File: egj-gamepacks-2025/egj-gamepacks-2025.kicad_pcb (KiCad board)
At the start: 2 copper layers, 55.7 x 32 mm, 44 parts, among them J1 USB_B_Micro, J3 SM03B-SRSS-TB, J5 GameBoy_GamePak_AGB-002, SW1 SW_Push, SW2 SW_Push, U1 W25Q128JVS, U2 DNF, U3 NCP1117-3.3_SOT223, U4 RP2350_80QFN, Y1 ABM8-272-T3

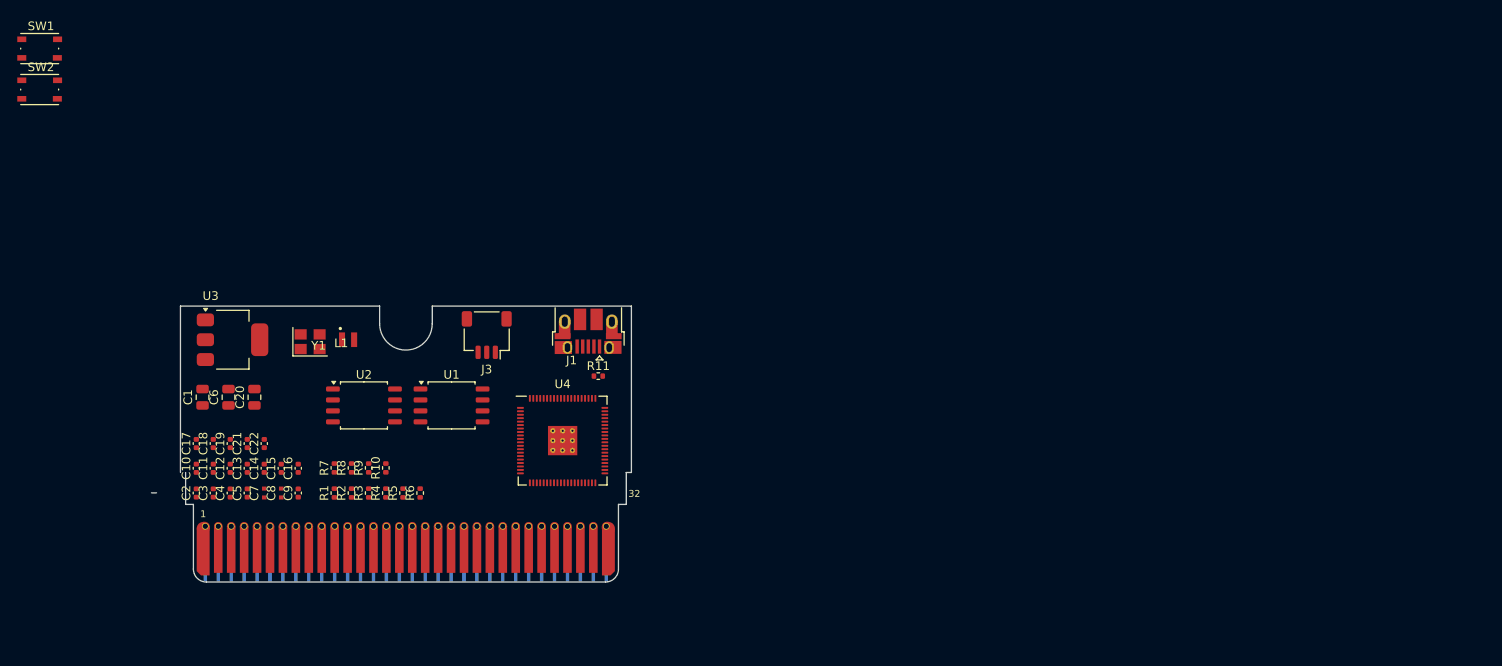
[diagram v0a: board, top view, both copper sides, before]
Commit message: add new schemas
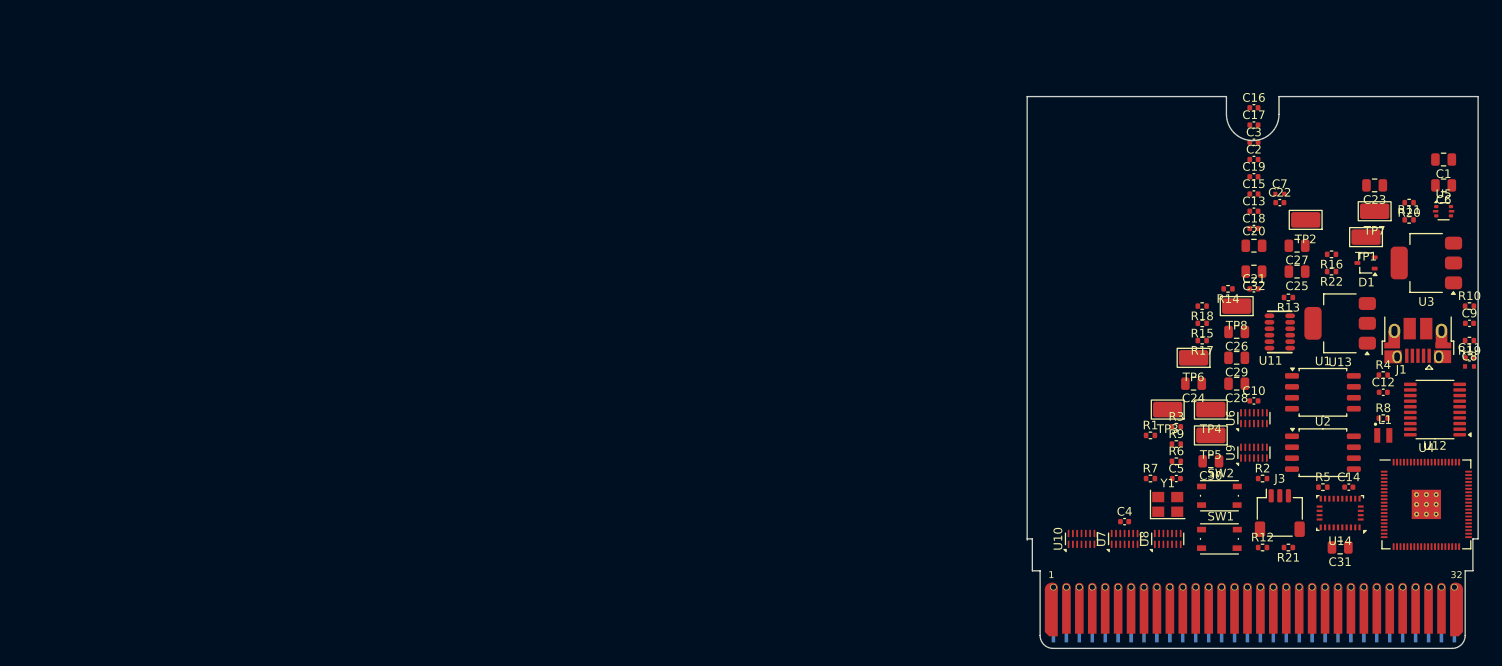
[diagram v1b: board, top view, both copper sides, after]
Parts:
- added C23: 100u, Capacitor_SMD:C_0805_2012Metric, F.Cu at (262.0, 71.0)
- added C24: 10u, Capacitor_SMD:C_0805_2012Metric, F.Cu at (241.0, 94.0)
- added C25: 100n, Capacitor_SMD:C_0805_2012Metric, F.Cu at (253.0, 81.0)
- added C26: 1u, Capacitor_SMD:C_0805_2012Metric, F.Cu at (246.0, 88.0)
- added C27: 1u, Capacitor_SMD:C_0805_2012Metric, F.Cu at (253.0, 78.0)
- added C28: 100n, Capacitor_SMD:C_0805_2012Metric, F.Cu at (246.0, 94.0)
- added C29: 4.7u, Capacitor_SMD:C_0805_2012Metric, F.Cu at (246.0, 91.0)
- added C30: 1u, Capacitor_SMD:C_0805_2012Metric, F.Cu at (243.0, 103.0)
- added C31: 120n, Capacitor_SMD:C_0805_2012Metric, F.Cu at (258.0, 113.0)
- added C32: 100n, Capacitor_SMD:C_0805_2012Metric, F.Cu at (248.0, 81.0)
- added D1: BAT54CW, Package_TO_SOT_SMD:SOT-323_SC-70, F.Cu at (261.0, 80.0)
- added R12: 10k, Resistor_SMD:R_0402_1005Metric, F.Cu at (249.0, 113.0)
- added R13: 4.7K, Resistor_SMD:R_0402_1005Metric, F.Cu at (252.0, 84.0)
- added R14: 4.7K, Resistor_SMD:R_0402_1005Metric, F.Cu at (245.0, 83.0)
- added R15: 33, Resistor_SMD:R_0402_1005Metric, F.Cu at (242.0, 87.0)
- added R16: 33, Resistor_SMD:R_0402_1005Metric, F.Cu at (257.0, 79.0)
- added R17: 4.7K, Resistor_SMD:R_0402_1005Metric, F.Cu at (242.0, 89.0)
- added R18: 4.7K, Resistor_SMD:R_0402_1005Metric, F.Cu at (242.0, 85.0)
- added R19: 4.7K, Resistor_SMD:R_0402_1005Metric, F.Cu at (273.0, 89.0)
- added R20: 10K, Resistor_SMD:R_0402_1005Metric, F.Cu at (266.0, 73.0)
- added R21: 4.7K, Resistor_SMD:R_0402_1005Metric, F.Cu at (252.0, 113.0)
- added R22: 10K, Resistor_SMD:R_0402_1005Metric, F.Cu at (257.0, 81.0)
- added TP1: TestPoint, TestPoint:TestPoint_Keystone_5015_Micro_Mini, F.Cu at (261.0, 77.0)
- added TP2: TestPoint, TestPoint:TestPoint_Keystone_5015_Micro_Mini, F.Cu at (254.0, 75.0)
- added TP3: TestPoint, TestPoint:TestPoint_Keystone_5015_Micro_Mini, F.Cu at (238.0, 97.0)
- added TP4: TestPoint, TestPoint:TestPoint_Keystone_5015_Micro_Mini, F.Cu at (243.0, 97.0)
- added TP5: TestPoint, TestPoint:TestPoint_Keystone_5015_Micro_Mini, F.Cu at (243.0, 100.0)
- added TP6: TestPoint, TestPoint:TestPoint_Keystone_5015_Micro_Mini, F.Cu at (241.0, 91.0)
- added TP7: TestPoint, TestPoint:TestPoint_Keystone_5015_Micro_Mini, F.Cu at (262.0, 74.0)
- added TP8: TestPoint, TestPoint:TestPoint_Keystone_5015_Micro_Mini, F.Cu at (246.0, 85.0)
- added U10: SP3012-06UTG, Package_DFN_QFN:DFN-14_1.35x3.5mm_P0.5mm, F.Cu at (228.0, 112.0)
- added U11: VL6180XV0NR_1, VL6180XV0NR_1:LGA12R75P2X6_280X480X110, F.Cu at (251.0, 88.0)
- added U12: TXS0108EPW, Package_SO:TSSOP-20_4.4x6.5mm_P0.65mm, F.Cu at (269.0, 97.0)
- added U13: LD1117S18TR_SOT223, Package_TO_SOT_SMD:SOT-223-3_TabPin2, F.Cu at (258.0, 87.0)
- added U14: BNO055, Package_LGA:LGA-28_5.2x3.8mm_P0.5mm, F.Cu at (258.0, 109.0)
- added U5: USBLC6-2P6, Package_TO_SOT_SMD:SOT-666, F.Cu at (270.0, 74.0)
- added U6: SP3012-06UTG, Package_DFN_QFN:DFN-14_1.35x3.5mm_P0.5mm, F.Cu at (248.0, 98.0)
- added U7: SP3012-06UTG, Package_DFN_QFN:DFN-14_1.35x3.5mm_P0.5mm, F.Cu at (233.0, 112.0)
- added U8: SP3012-06UTG, Package_DFN_QFN:DFN-14_1.35x3.5mm_P0.5mm, F.Cu at (238.0, 112.0)
- added U9: SP3012-06UTG, Package_DFN_QFN:DFN-14_1.35x3.5mm_P0.5mm, F.Cu at (248.0, 102.0)
- U1, U2: footprint Package_SO:SOIC-8_5.23x5.23mm_P1.27mm -> Package_SO:SOIC-8_5.3x5.3mm_P1.27mm
- moved SW1 148.2 mm to (244.0, 112.0)
- moved C1 146.6 mm to (270.0, 68.0), turned to 180 degrees
- moved C11 146.3 mm to (273.0, 91.0), turned to 0 degrees
- moved SW2 144.7 mm to (244.0, 107.0)
- moved C6 143.1 mm to (270.0, 71.0), turned to 180 degrees
- moved U3 138.7 mm to (268.0, 80.0), turned to 180 degrees
- moved C8 138.6 mm to (273.0, 92.0), turned to 0 degrees
- moved C9 137.3 mm to (273.0, 87.0), turned to 0 degrees
- moved C12 134.0 mm to (263.0, 95.0), turned to 0 degrees
- moved C2 128.6 mm to (248.0, 68.0), turned to 0 degrees
- moved C17 128.1 mm to (248.0, 64.0), turned to 0 degrees
- moved C3 127.4 mm to (248.0, 66.0), turned to 0 degrees
- moved R10 127.1 mm to (273.0, 85.0), turned to 0 degrees
- moved C14 125.8 mm to (259.0, 106.0), turned to 0 degrees
- moved C18 123.2 mm to (248.0, 76.0), turned to 0 degrees
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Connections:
- net /FLASH2_SS renamed /RP2350/FLASH2_SS
- net /FLASH_SS renamed /RP2350/FLASH_SS
- net /GPIO28 renamed /GBA_Connector/GBA_SIG.N_CS2
- net /GPIO29 renamed /GBA_Connector/GBA_SIG.IRQ
- net /QSPI_SCLK renamed /RP2350/QSPI_SCLK
- net /QSPI_SD0 renamed /RP2350/QSPI_SD0
- net /QSPI_SD1 renamed /RP2350/QSPI_SD1
- net /QSPI_SD2 renamed /RP2350/QSPI_SD2
- net /QSPI_SD3 renamed /RP2350/QSPI_SD3
- net /QSPI_SS renamed /RP2350/QSPI_SS
- net /RUN renamed /RP2350/RUN
- net /SWCLK renamed /RP2350/SWCLK
- net /SWD renamed /RP2350/SWD
- net /VREG_AVDD renamed Net-(U4-VREG_AVDD)
- net /VREG_LX renamed /RP2350/VREG_LX
- net /XIN renamed /RP2350/XIN
- net /XOUT renamed /RP2350/XOUT
- net /~{USB_BOOT} renamed /RP2350/~{USB_BOOT}
- C6 pad 1: +3V3 -> +3V3_USB
- J1 pad 2: /USB_D- -> /Power/USB.USB_D_C-
- J1 pad 3: /USB_D+ -> /Power/USB.USB_D_C+
- J5 pad 1: +3.3V -> +3V3_GBA
- J5 pad 10: /GPIO8 -> /GBA_Connector/GBA_ADD4
- J5 pad 11: /GPIO9 -> /GBA_Connector/GBA_ADD5
- J5 pad 12: /GPIO10 -> /GBA_Connector/GBA_ADD6
- J5 pad 13: /GPIO11 -> /GBA_Connector/GBA_ADD7
- J5 pad 14: /GPIO12 -> /GBA_Connector/GBA_ADD8
- J5 pad 15: /GPIO13 -> /GBA_Connector/GBA_ADD9
- J5 pad 16: /GPIO14 -> /GBA_Connector/GBA_ADD10
- J5 pad 17: /GPIO15 -> /GBA_Connector/GBA_ADD11
- J5 pad 18: /GPIO16 -> /GBA_Connector/GBA_ADD12
- J5 pad 19: /GPIO17 -> /GBA_Connector/GBA_ADD13
- J5 pad 2: /GPIO0 -> /GBA_Connector/GBA_SIG.PHI
- J5 pad 20: /GPIO18 -> /GBA_Connector/GBA_ADD14
- J5 pad 21: /GPIO19 -> /GBA_Connector/GBA_ADD15
- J5 pad 22: /GPIO20 -> /GBA_Connector/GBA_DATA0
- J5 pad 23: /GPIO21 -> /GBA_Connector/GBA_DATA1
- J5 pad 24: /GPIO22 -> /GBA_Connector/GBA_DATA2
- J5 pad 25: /GPIO23 -> /GBA_Connector/GBA_DATA3
- J5 pad 26: /GPIO24 -> /GBA_Connector/GBA_DATA4
- J5 pad 27: /GPIO25 -> /GBA_Connector/GBA_DATA5
- J5 pad 28: /GPIO26 -> /GBA_Connector/GBA_DATA6
- J5 pad 29: /GPIO27 -> /GBA_Connector/GBA_DATA7
- J5 pad 3: /GPIO1 -> /GBA_Connector/GBA_SIG.N_WR
- J5 pad 4: /GPIO2 -> /GBA_Connector/GBA_SIG.N_RD
- J5 pad 5: /GPIO3 -> /GBA_Connector/GBA_SIG.N_CS
- J5 pad 6: /GPIO4 -> /GBA_Connector/GBA_ADD0
- J5 pad 7: /GPIO5 -> /GBA_Connector/GBA_ADD1
- J5 pad 8: /GPIO6 -> /GBA_Connector/GBA_ADD2
- J5 pad 9: /GPIO7 -> /GBA_Connector/GBA_ADD3
- R1 pad 1: /GPIO0 -> /RP2350/GPIO0
- R10 pad 1: /USB_D+ -> /RP2350/USB_D+
- R11 pad 1: /USB_D- -> /RP2350/USB_D-
- R3 pad 1: /GPIO0 -> /RP2350/GPIO0
- U3 pad 2: +3V3 -> +3V3_USB
- U4 pad 1: /GPIO4 -> /GBA_Connector/GBA_DATA4
- U4 pad 11: /GPIO12 -> /GBA_Connector/GBA_ADD4
- U4 pad 12: /GPIO13 -> /GBA_Connector/GBA_ADD5
- U4 pad 13: /GPIO14 -> /GBA_Connector/GBA_ADD6
- U4 pad 14: /GPIO15 -> /GBA_Connector/GBA_ADD7
- U4 pad 16: /GPIO16 -> /GBA_Connector/GBA_ADD8
- U4 pad 17: /GPIO17 -> /GBA_Connector/GBA_ADD9
- U4 pad 18: /GPIO18 -> /GBA_Connector/GBA_ADD10
- U4 pad 19: /GPIO19 -> /GBA_Connector/GBA_ADD11
- U4 pad 2: /GPIO5 -> /GBA_Connector/GBA_DATA5
- U4 pad 20: /GPIO20 -> /GBA_Connector/GBA_ADD12
- U4 pad 21: /GPIO21 -> /GBA_Connector/GBA_ADD13
- U4 pad 22: /GPIO22 -> /GBA_Connector/GBA_ADD14
- U4 pad 23: /GPIO23 -> /GBA_Connector/GBA_ADD15
- U4 pad 25: /GPIO24 -> /GBA_Connector/GBA_SIG.PHI
- U4 pad 26: /GPIO25 -> /GBA_Connector/GBA_SIG.N_WR
- U4 pad 27: /GPIO26 -> /GBA_Connector/GBA_SIG.N_RD
- U4 pad 28: /GPIO27 -> /GBA_Connector/GBA_SIG.N_CS
- U4 pad 3: /GPIO6 -> /GBA_Connector/GBA_DATA6
- U4 pad 38: /GPIO30 -> /RP2350/VL6180XV0NR_I2C.SDA
- U4 pad 39: /GPIO31 -> /RP2350/VL6180XV0NR_I2C.SCL
- U4 pad 4: /GPIO7 -> /GBA_Connector/GBA_DATA7
- U4 pad 40: /GPIO32 -> /RP2350/VL6180XV0NR_I2C.GPIO0
- U4 pad 42: /GPIO33 -> /RP2350/VL6180XV0NR_I2C.GPIO1
- U4 pad 43: /GPIO34 -> unconnected-(U4-GPIO34-Pad43)
- U4 pad 44: /GPIO35 -> /RP2350/BNO055_UART.TX
- U4 pad 45: /GPIO36 -> /RP2350/BNO055_UART.RX
- U4 pad 46: /GPIO37 -> /RP2350/BNO055_UART.INT
- U4 pad 47: /GPIO38 -> /RP2350/BNO055_UART.RESET
- U4 pad 48: /GPIO39 -> /RP2350/BNO055_UART.BL_IND
- U4 pad 49: /GPIO40_ADC0 -> unconnected-(U4-GPIO40_ADC0-Pad49)
- U4 pad 52: /GPIO41_ADC1 -> unconnected-(U4-GPIO41_ADC1-Pad52)
- U4 pad 53: /GPIO42_ADC2 -> unconnected-(U4-GPIO42_ADC2-Pad53)
- U4 pad 54: /GPIO43_ADC3 -> unconnected-(U4-GPIO43_ADC3-Pad54)
- U4 pad 55: /GPIO44_ADC4 -> unconnected-(U4-GPIO44_ADC4-Pad55)
- U4 pad 56: /GPIO45_ADC5 -> unconnected-(U4-GPIO45_ADC5-Pad56)
- U4 pad 57: /GPIO46_ADC6 -> +3V3_GBA
- U4 pad 58: /GPIO47_ADC7 -> +3V3_USB
- U4 pad 6: /GPIO8 -> /GBA_Connector/GBA_ADD0
- U4 pad 7: /GPIO9 -> /GBA_Connector/GBA_ADD1
- U4 pad 77: /GPIO0 -> /GBA_Connector/GBA_DATA0
- U4 pad 78: /GPIO1 -> /GBA_Connector/GBA_DATA1
- U4 pad 79: /GPIO2 -> /GBA_Connector/GBA_DATA2
- U4 pad 8: /GPIO10 -> /GBA_Connector/GBA_ADD2
- U4 pad 80: /GPIO3 -> /GBA_Connector/GBA_DATA3
- U4 pad 9: /GPIO11 -> /GBA_Connector/GBA_ADD3
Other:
- board size 55.7 x 32 mm -> 52.3 x 64 mm

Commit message: Update
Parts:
- removed J3: SM03B-SRSS-TB, Connector_JST:JST_SH_SM03B-SRSS-TB_1x03-1MP_P1.00mm_Horizontal
- removed TP1, TP2, TP7, TP8: TestPoint, TestPoint:TestPoint_Keystone_5015_Micro_Mini
- added J2: Conn_01x03_Pin, Connector_PinHeader_2.54mm:PinHeader_1x03_P2.54mm_Horizontal, F.Cu at (119.0, 66.0)
- added U15: SP3012-06UTG, Package_DFN_QFN:DFN-14_1.35x3.5mm_P0.5mm, F.Cu at (165.0, 113.0)
- moved C9 140.2 mm to (133.2, 96.6), turned to 180 degrees
- moved C11 139.9 mm to (133.2, 94.6), turned to 180 degrees
- moved C8 139.9 mm to (133.1, 93.6), turned to 180 degrees
- moved R4 139.5 mm to (123.5, 94.0), turned to 180 degrees
- moved R19 133.6 mm to (139.6, 81.9), turned to 90 degrees
- moved R5 132.5 mm to (123.5, 102.5), turned to 180 degrees
- moved U1 131.5 mm to (124.5, 97.5)
- moved U2 131.5 mm to (124.6, 105.9)
- moved C12 129.8 mm to (133.2, 95.6), turned to 180 degrees
- moved R2 129.0 mm to (120.5, 94.0)
- moved SW1 128.6 mm to (125.5, 62.0)
- moved C3 127.8 mm to (125.5, 102.5)
- moved L1 127.4 mm to (135.7, 96.1)
- moved R10 126.7 mm to (147.4, 68.0), turned to -90 degrees
- moved U12 125.5 mm to (144.1, 84.4), turned to -90 degrees
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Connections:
- net +1V1 renamed /RP2350/+1V1
- D1 pad 1: +3V3_GBA -> +3V3_USB
- D1 pad 2: +3V3_USB -> +3V3_GBA
- R10 pad 1: /RP2350/USB_D+ -> /Power/USB.USB_D_C+
- R11 pad 1: /RP2350/USB_D- -> /Power/USB.USB_D_C-
- U10 pad 1: unconnected-(U10-Pad1) -> /GBA_Connector/GBA_ADD13
- U10 pad 11: /GBA_Connector/GBA_SIG.N_CS -> /GBA_Connector/GBA_DATA0
- U10 pad 12: /GBA_Connector/GBA_SIG.N_RD -> /GBA_Connector/GBA_ADD15
- U10 pad 13: /GBA_Connector/GBA_SIG.N_WR -> /GBA_Connector/GBA_ADD14
- U10 pad 14: /GBA_Connector/GBA_SIG.PHI -> /GBA_Connector/GBA_ADD13
- U10 pad 2: unconnected-(U10-Pad2) -> /GBA_Connector/GBA_ADD14
- U10 pad 3: unconnected-(U10-Pad3) -> /GBA_Connector/GBA_ADD15
- U10 pad 4: unconnected-(U10-Pad4) -> /GBA_Connector/GBA_DATA0
- U10 pad 5: unconnected-(U10-Pad5) -> GND
- U10 pad 6: unconnected-(U10-Pad6) -> /GBA_Connector/GBA_DATA1
- U10 pad 7: unconnected-(U10-Pad7) -> /GBA_Connector/GBA_DATA2
- U10 pad 8: /GBA_Connector/GBA_SIG.IRQ -> /GBA_Connector/GBA_DATA2
- U10 pad 9: /GBA_Connector/GBA_SIG.N_CS2 -> /GBA_Connector/GBA_DATA1
- U4 pad 1: /GBA_Connector/GBA_DATA4 -> /GBA_Connector/GBA_ADD0
- U4 pad 11: /GBA_Connector/GBA_ADD4 -> /GBA_Connector/GBA_ADD8
- U4 pad 12: /GBA_Connector/GBA_ADD5 -> /GBA_Connector/GBA_ADD9
- U4 pad 13: /GBA_Connector/GBA_ADD6 -> /GBA_Connector/GBA_ADD10
- U4 pad 14: /GBA_Connector/GBA_ADD7 -> /GBA_Connector/GBA_ADD11
- U4 pad 16: /GBA_Connector/GBA_ADD8 -> /GBA_Connector/GBA_ADD12
- U4 pad 17: /GBA_Connector/GBA_ADD9 -> /GBA_Connector/GBA_ADD13
- U4 pad 18: /GBA_Connector/GBA_ADD10 -> /GBA_Connector/GBA_ADD14
- U4 pad 19: /GBA_Connector/GBA_ADD11 -> /GBA_Connector/GBA_ADD15
- U4 pad 2: /GBA_Connector/GBA_DATA5 -> /GBA_Connector/GBA_ADD1
- U4 pad 20: /GBA_Connector/GBA_ADD12 -> /GBA_Connector/GBA_DATA0
- U4 pad 21: /GBA_Connector/GBA_ADD13 -> /GBA_Connector/GBA_DATA1
- U4 pad 22: /GBA_Connector/GBA_ADD14 -> /GBA_Connector/GBA_DATA2
- U4 pad 23: /GBA_Connector/GBA_ADD15 -> /GBA_Connector/GBA_DATA3
- U4 pad 25: /GBA_Connector/GBA_SIG.PHI -> /GBA_Connector/GBA_DATA4
- U4 pad 26: /GBA_Connector/GBA_SIG.N_WR -> /GBA_Connector/GBA_DATA5
- U4 pad 27: /GBA_Connector/GBA_SIG.N_RD -> /GBA_Connector/GBA_DATA6
- U4 pad 28: /GBA_Connector/GBA_SIG.N_CS -> /GBA_Connector/GBA_DATA7
- U4 pad 3: /GBA_Connector/GBA_DATA6 -> /GBA_Connector/GBA_ADD2
- U4 pad 4: /GBA_Connector/GBA_DATA7 -> /GBA_Connector/GBA_ADD3
- U4 pad 6: /GBA_Connector/GBA_ADD0 -> /GBA_Connector/GBA_ADD4
- U4 pad 7: /GBA_Connector/GBA_ADD1 -> /GBA_Connector/GBA_ADD5
- U4 pad 77: /GBA_Connector/GBA_DATA0 -> /GBA_Connector/GBA_SIG.PHI
- U4 pad 78: /GBA_Connector/GBA_DATA1 -> /GBA_Connector/GBA_SIG.N_WR
- U4 pad 79: /GBA_Connector/GBA_DATA2 -> /GBA_Connector/GBA_SIG.N_RD
- U4 pad 8: /GBA_Connector/GBA_ADD2 -> /GBA_Connector/GBA_ADD6
- U4 pad 80: /GBA_Connector/GBA_DATA3 -> /GBA_Connector/GBA_SIG.N_CS
- U4 pad 9: /GBA_Connector/GBA_ADD3 -> /GBA_Connector/GBA_ADD7
- U5 pad 2: GND -> unconnected-(U5-GND-Pad2)
- U5 pad 4: /RP2350/USB_D- -> /Power/USB.USB_D_C-
- U5 pad 5: unconnected-(U5-VBUS-Pad5) -> GND
- U5 pad 6: /RP2350/USB_D+ -> /Power/USB.USB_D_C+
- U6 pad 1: unconnected-(U6-Pad1) -> /GBA_Connector/GBA_DATA3
- U6 pad 11: /GBA_Connector/GBA_DATA3 -> /GBA_Connector/GBA_DATA6
- U6 pad 12: /GBA_Connector/GBA_DATA2 -> /GBA_Connector/GBA_DATA5
- U6 pad 13: /GBA_Connector/GBA_DATA1 -> /GBA_Connector/GBA_DATA4
- U6 pad 14: /GBA_Connector/GBA_DATA0 -> /GBA_Connector/GBA_DATA3
- U6 pad 2: unconnected-(U6-Pad2) -> /GBA_Connector/GBA_DATA4
- U6 pad 3: unconnected-(U6-Pad3) -> /GBA_Connector/GBA_DATA5
- U6 pad 4: unconnected-(U6-Pad4) -> /GBA_Connector/GBA_DATA6
- U6 pad 5: unconnected-(U6-Pad5) -> GND
- U6 pad 6: unconnected-(U6-Pad6) -> /GBA_Connector/GBA_DATA7
- U6 pad 7: unconnected-(U6-Pad7) -> /GBA_Connector/GBA_SIG.N_CS2
- U6 pad 8: /GBA_Connector/GBA_DATA5 -> /GBA_Connector/GBA_SIG.N_CS2
- U6 pad 9: /GBA_Connector/GBA_DATA4 -> /GBA_Connector/GBA_DATA7
- U7 pad 1: unconnected-(U7-Pad1) -> /GBA_Connector/GBA_SIG.PHI
- U7 pad 11: /GBA_Connector/GBA_ADD1 -> /GBA_Connector/GBA_SIG.N_CS
- U7 pad 12: /GBA_Connector/GBA_ADD0 -> /GBA_Connector/GBA_SIG.N_RD
- U7 pad 13: /GBA_Connector/GBA_DATA7 -> /GBA_Connector/GBA_SIG.N_WR
- U7 pad 14: /GBA_Connector/GBA_DATA6 -> /GBA_Connector/GBA_SIG.PHI
- U7 pad 2: unconnected-(U7-Pad2) -> /GBA_Connector/GBA_SIG.N_WR
- U7 pad 3: unconnected-(U7-Pad3) -> /GBA_Connector/GBA_SIG.N_RD
- U7 pad 4: unconnected-(U7-Pad4) -> /GBA_Connector/GBA_SIG.N_CS
- U7 pad 5: unconnected-(U7-Pad5) -> GND
- U7 pad 6: unconnected-(U7-Pad6) -> /GBA_Connector/GBA_ADD0
- U7 pad 7: unconnected-(U7-Pad7) -> /GBA_Connector/GBA_ADD1
- U7 pad 8: /GBA_Connector/GBA_ADD3 -> /GBA_Connector/GBA_ADD1
- U7 pad 9: /GBA_Connector/GBA_ADD2 -> /GBA_Connector/GBA_ADD0
- U8 pad 1: unconnected-(U8-Pad1) -> /GBA_Connector/GBA_ADD2
- U8 pad 11: /GBA_Connector/GBA_ADD7 -> /GBA_Connector/GBA_ADD4
- U8 pad 12: /GBA_Connector/GBA_ADD6 -> /GBA_Connector/GBA_ADD3
- U8 pad 13: /GBA_Connector/GBA_ADD5 -> /GBA_Connector/GBA_ADD2
- U8 pad 14: /GBA_Connector/GBA_ADD4 -> /GBA_Connector/GBA_ADD2
- U8 pad 2: unconnected-(U8-Pad2) -> /GBA_Connector/GBA_ADD2
- U8 pad 3: unconnected-(U8-Pad3) -> /GBA_Connector/GBA_ADD3
- U8 pad 4: unconnected-(U8-Pad4) -> /GBA_Connector/GBA_ADD4
- U8 pad 5: unconnected-(U8-Pad5) -> GND
- U8 pad 6: unconnected-(U8-Pad6) -> /GBA_Connector/GBA_ADD5
- U8 pad 7: unconnected-(U8-Pad7) -> /GBA_Connector/GBA_ADD6
- U8 pad 8: /GBA_Connector/GBA_ADD9 -> /GBA_Connector/GBA_ADD6
- U8 pad 9: /GBA_Connector/GBA_ADD8 -> /GBA_Connector/GBA_ADD5
- U9 pad 1: unconnected-(U9-Pad1) -> /GBA_Connector/GBA_ADD7
- U9 pad 11: /GBA_Connector/GBA_ADD13 -> /GBA_Connector/GBA_ADD10
- U9 pad 12: /GBA_Connector/GBA_ADD12 -> /GBA_Connector/GBA_ADD9
- U9 pad 13: /GBA_Connector/GBA_ADD11 -> /GBA_Connector/GBA_ADD8
- U9 pad 14: /GBA_Connector/GBA_ADD10 -> /GBA_Connector/GBA_ADD7
- U9 pad 2: unconnected-(U9-Pad2) -> /GBA_Connector/GBA_ADD8
- U9 pad 3: unconnected-(U9-Pad3) -> /GBA_Connector/GBA_ADD9
- U9 pad 4: unconnected-(U9-Pad4) -> /GBA_Connector/GBA_ADD10
- U9 pad 5: unconnected-(U9-Pad5) -> GND
- U9 pad 6: unconnected-(U9-Pad6) -> /GBA_Connector/GBA_ADD11
- U9 pad 7: unconnected-(U9-Pad7) -> /GBA_Connector/GBA_ADD12
- U9 pad 8: /GBA_Connector/GBA_ADD15 -> /GBA_Connector/GBA_ADD12
- U9 pad 9: /GBA_Connector/GBA_ADD14 -> /GBA_Connector/GBA_ADD11
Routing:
- net +3V3: track 0.00 -> 55.3 mm
- net VBUS: track 0.00 -> 21.7 mm
- net +3V3_USB: track 0.00 -> 17.0 mm
- net +1V8: track 0.00 -> 8.68 mm
- net +3V3_GBA: track 0.00 -> 1.87 mm
- net (no net): vias 0 -> 1
- added copper zone on B.Cu, net (none)
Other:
- outline, holes or cut-outs redrawn
